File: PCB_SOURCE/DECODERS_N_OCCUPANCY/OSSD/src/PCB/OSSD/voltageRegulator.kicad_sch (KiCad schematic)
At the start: 7 parts

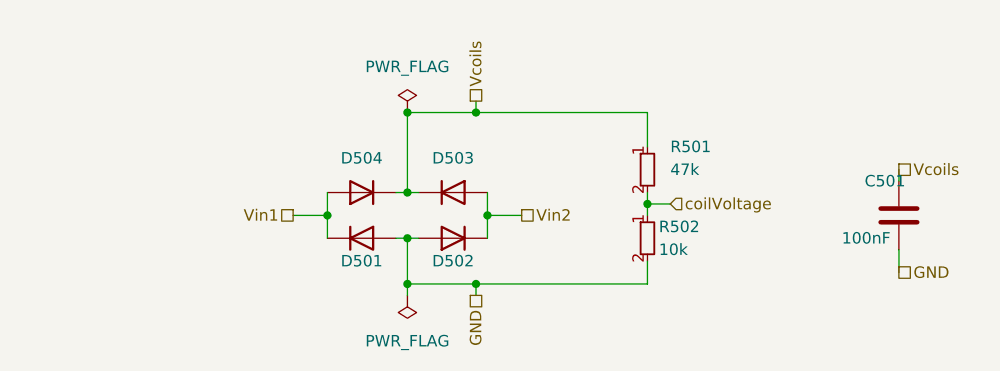
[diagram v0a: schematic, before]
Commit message: added S88 current sense to releases and update OSSD decoder
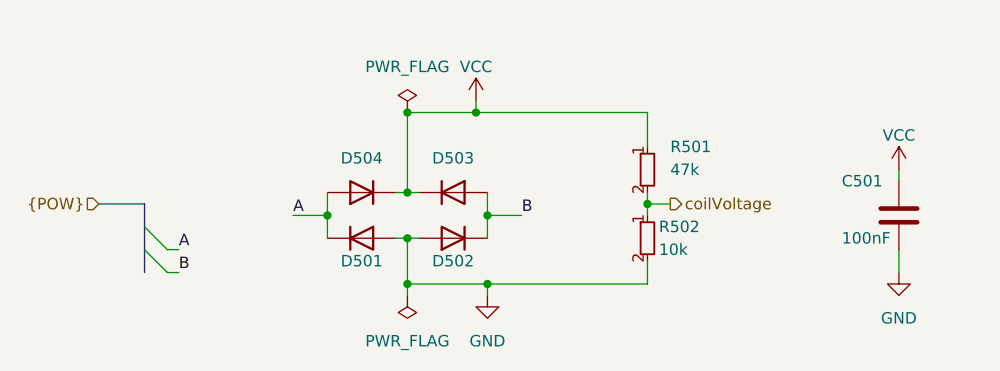
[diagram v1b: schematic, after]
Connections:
- net Vcoils renamed VCC
- net Vin1 renamed A
- net Vin2 renamed B
